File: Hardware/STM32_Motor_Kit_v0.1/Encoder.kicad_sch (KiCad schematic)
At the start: 26 parts, among them J5 Conn_01x05_Male, U13 LSF0204DPWR

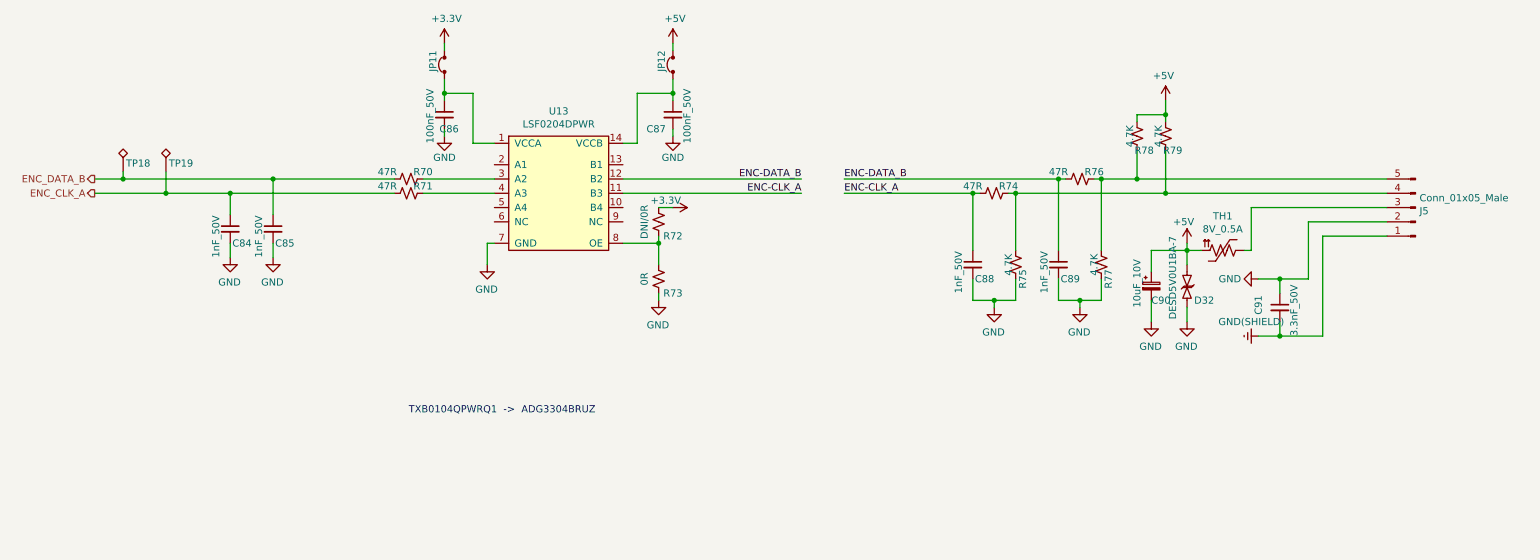
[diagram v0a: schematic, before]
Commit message: Şemada güncellemeler yaptım, PCB'de revizyon yapılacak
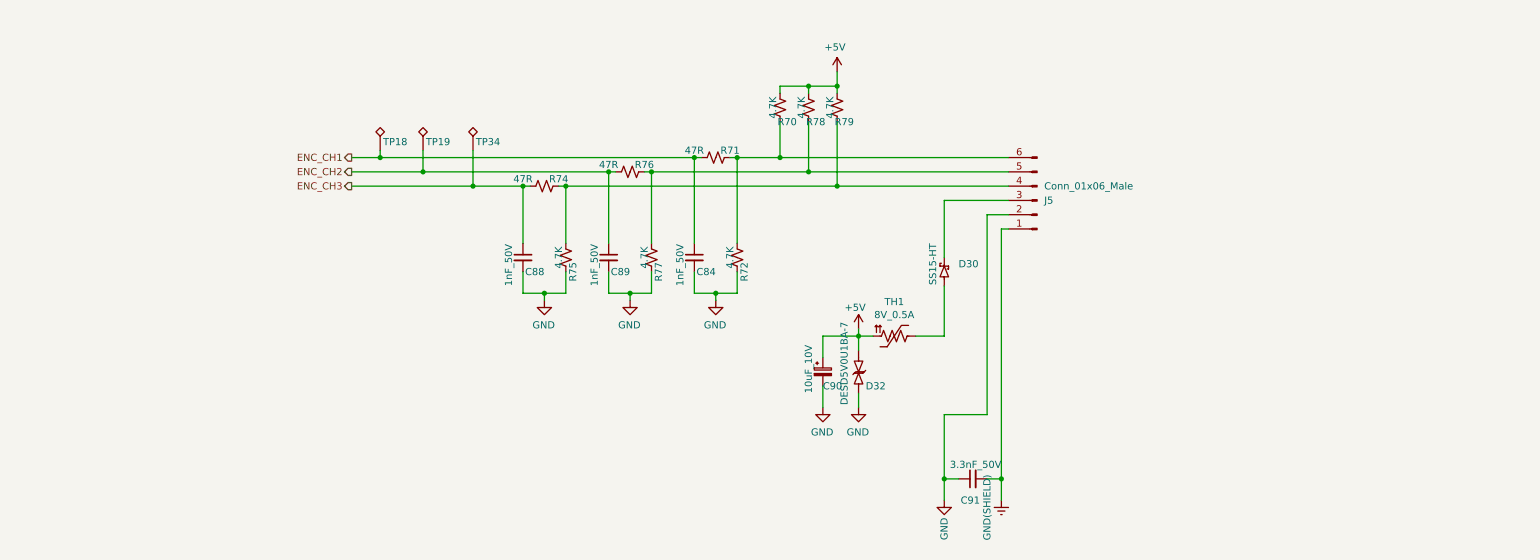
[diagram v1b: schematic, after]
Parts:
- removed C85: 1nF_50V, AKE_Capacitor_SMD:CAP_0603, symbol AKE_Capacitor:Capacitor_UnPolarised
- removed C86, C87: 100nF_50V, AKE_Capacitor_SMD:CAP_0603, symbol AKE_Capacitor:Capacitor_UnPolarised
- removed J5: Conn_01x05_Male, AKE_Connector_W2B:TerminalBlock_Phoenix_MKDS-1,5-5_1x05_P5.00mm_Horizontal, symbol AKE_Connector_Socket:Conn_01x05_Male
- removed JP11, JP12: Jumper_Pinheader, AKE_Pinheader_TH:PinHeader_1x02_P2.54mm_Vertical, symbol AKE_Device:Jumper_Pinheader
- removed R73: 0R, AKE_Resistor_SMD:RES_0603, symbol AKE_Resistor:Resistor_US
- removed U13: LSF0204DPWR, AKE_IC_SMD:TSSOP-14_4.4x5mm_P0.65mm, symbol AKE_IC:LSF0204DPWR
- added D30: SS15-HT, AKE_Diode_SMD:SMA, symbol AKE_Diode:Diode_Schottky
- added J5: Conn_01x06_Male, AKE_Connector_W2B:TerminalBlock_Phoenix_MKDS-1,5-6_1x06_P5.00mm_Horizontal, symbol AKE_Connector_Socket:Conn_01x06_Male
- added TP34: Test_Point, AKE_PCB:TEST_POINT, symbol AKE_Device:Test_Point
- R70: value 47R -> 4.7K
- R72: value DNI/0R -> 4.7K
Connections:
- net +3.3V is gone; now on net GND: R72.1
- net +5V: now also R70.2
- net GND: now also J5.2 (Pin_2)
- net GND(SHIELD): now also J5.1 (Pin_1)
- net at R76.1, R77.2, R78.1: now also J5.5 (Pin_5)
- net at R72.2: now also R70.1, R71.1, J5.6 (Pin_6)
- net at TH1.1: now also D30.2
- net at R74.1, R75.2, R79.1: now also J5.4 (Pin_4)
- net ENC-CLK_A renamed ENC_CH3
- net ENC_CH3: now also TP34.1
- net ENC-DATA_B renamed ENC_CH2
- net ENC_CH2: now also TP19.1
- net ENC_CLK_A renamed ENC_CH1
- net ENC_CH1: now also TP18.1; no longer TP19.1
- removed net ENC_DATA_B: R70.2, TP18.1
- new net: D30.1, J5.3 (Pin_3)
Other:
- note removed: "TXB0104QPWRQ1 -> ADG3304BRUZ"
- moved on the sheet: C88, C89, C90, C91, D32, R74, R75, R76, R77, R78, R79, TH1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

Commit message: 16.09.2024
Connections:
- net GND: now also J5.5 (Pin_5); no longer J5.2 (Pin_2)
- net GND(SHIELD): now also J5.6 (Pin_6); no longer J5.1 (Pin_1)
- net at D30.1: now also J5.4 (Pin_4); no longer J5.3 (Pin_3)
- net at R76.1, R77.2, R78.1: now also J5.2 (Pin_2); no longer J5.5 (Pin_5)
- net at R70.1, R71.1, R72.2: now also J5.1 (Pin_1); no longer J5.6 (Pin_6)
- net at R74.1, R75.2, R79.1: now also J5.3 (Pin_3); no longer J5.4 (Pin_4)
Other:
- moved on the sheet: J5
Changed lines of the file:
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@@
 	(symbol
 		(lib_id "AKE_Connector_Socket:Conn_01x06_Male")
-		(at 200.66 85.09 180)
+		(at 200.66 82.55 0)
+		(mirror y)
 		(unit 1)
 		(exclude_from_sim no)
@@
 		(dnp no)
 		(property "Reference" "J5"
-			(at 201.93 85.0901 0)
+			(at 201.93 82.5499 0)
 			(effects
 				(font
@@
 		)
 		(property "Value" "Conn_01x06_Male"
-			(at 201.93 82.5501 0)
+			(at 201.93 85.0899 0)
 			(effects
 				(font
@@
 		)
 		(property "Footprint" "AKE_Connector_W2B:TerminalBlock_Phoenix_MKDS-1,5-6_1x06_P5.00mm_Horizontal"
-			(at 200.66 85.09 0)
+			(at 200.66 82.55 0)
 			(effects
 				(font
@@
 		)
 		(property "Datasheet" "~"
-			(at 200.66 85.09 0)
+			(at 200.66 82.55 0)
 			(effects
 				(font
@@
 		)
 		(property "Description" "Generic connector, single row, 01x06, script generated (kicad-library-utils/schlib/autogen/connector/)"
-			(at 200.66 85.09 0)
+			(at 200.66 82.55 0)
 			(effects
 				(font

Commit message: 12.01.2025
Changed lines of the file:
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@@
 			(effects
 				(font
-					(size 1.27 1.27)
+					(face "Arial")
+					(size 0.635 0.635)
 				)
 				(justify left)
@@
 			(effects
 				(font
-					(size 1.27 1.27)
+					(face "Arial")
+					(size 0.635 0.635)
 				)
 				(hide yes)
@@
 			(effects
 				(font
-					(size 1.27 1.27)
+					(face "Arial")
+					(size 0.635 0.635)
 				)
 				(justify left)
@@
 			(effects
 				(font
-					(size 1.27 1.27)
+					(face "Arial")
+					(size 0.635 0.635)
 				)
 				(hide yes)
@@
 			(effects
 				(font
-					(size 1.27 1.27)
+					(face "Arial")
+					(size 0.635 0.635)
 				)
 				(justify left)
@@
 			(effects
 				(font
-					(size 1.27 1.27)
+					(face "Arial")
+					(size 0.635 0.635)
 				)
 				(hide yes)
@@
 			(effects
 				(font
-					(size 1.27 1.27)
+					(face "Arial")
+					(size 0.635 0.635)
 				)
 			)
@@
 			(effects
 				(font
-					(size 1.27 1.27)
+					(face "Arial")
+					(size 0.635 0.635)
 				)
 				(justify left)
@@
 			(effects
 				(font
-					(size 1.27 1.27)
+					(face "Arial")
+					(size 0.635 0.635)
 				)
 				(justify left)
@@
 			(effects
 				(font
-					(size 1.27 1.27)
+					(face "Arial")
+					(size 0.635 0.635)
 				)
 				(hide yes)
@@
 			(effects
 				(font
-					(size 1.27 1.27)
+					(face "Arial")
+					(size 0.635 0.635)
 				)
 				(justify left)
@@
 			(effects
 				(font
-					(size 1.27 1.27)
+					(face "Arial")
+					(size 0.635 0.635)
 				)
 			)
@@
 			(effects
 				(font
-					(size 1.27 1.27)
+					(face "Arial")
+					(size 0.635 0.635)
 				)
 				(justify left)
@@
 			(effects
 				(font
-					(size 1.27 1.27)
+					(face "Arial")
+					(size 0.635 0.635)
 				)
 				(hide yes)
@@
 			(effects
 				(font
-					(size 1.27 1.27)
+					(face "Arial")
+					(size 0.635 0.635)
 				)
 				(hide yes)
@@
 			(effects
 				(font
-					(size 1.27 1.27)
+					(face "Arial")
+					(size 0.635 0.635)
 				)
 				(hide yes)
@@
 			(effects
 				(font
-					(size 1.27 1.27)
+					(face "Arial")
+					(size 0.635 0.635)
 				)
 			)
@@
 			(effects
 				(font
-					(size 1.27 1.27)
+					(face "Arial")
+					(size 0.635 0.635)
 				)
 				(justify left)
@@
 			(effects
 				(font
-					(size 1.27 1.27)
+					(face "Arial")
+					(size 0.635 0.635)
 				)
 			)
@@
 			(effects
 				(font
-					(size 1.27 1.27)
+					(face "Arial")
+					(size 0.635 0.635)
 				)
 				(hide yes)
@@
 			(effects
 				(font
-					(size 1.27 1.27)
+					(face "Arial")
+					(size 0.635 0.635)
 				)
 			)
@@
 			(effects
 				(font
-					(size 1.27 1.27)
+					(face "Arial")
+					(size 0.635 0.635)
 				)
 			)
@@
 			(effects
 				(font
-					(size 1.27 1.27)
+					(face "Arial")
+					(size 0.635 0.635)
 				)
 				(justify right)
@@
 			(effects
 				(font
-					(size 1.27 1.27)
+					(face "Arial")
+					(size 0.635 0.635)
 				)
 			)
@@
 			(effects
 				(font
-					(size 1.27 1.27)
+					(face "Arial")
+					(size 0.635 0.635)
 				)
 			)
@@
 			(effects
 				(font
-					(size 1.27 1.27)
+					(face "Arial")
+					(size 0.635 0.635)
 				)
 			)
@@
 			(effects
 				(font
-					(size 1.27 1.27)
+					(face "Arial")
+					(size 0.635 0.635)
 				)
 				(justify left)
@@
 			(effects
 				(font
-					(size 1.27 1.27)
+					(face "Arial")
+					(size 0.635 0.635)
 				)
 				(justify left)
@@
 			(effects
 				(font
-					(size 1.27 1.27)
+					(face "Arial")
+					(size 0.635 0.635)
 				)
 				(hide yes)
@@
 			(effects
 				(font
-					(size 1.27 1.27)
-				)
-			)
+					(face "Arial")
+					(size 0.635 0.635)
+				)
+			)
